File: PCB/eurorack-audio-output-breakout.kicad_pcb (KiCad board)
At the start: 2 copper layers, 18.4 x 50.5 mm, 12 parts, among them J1 Conn_01x04_Pin, J10 A, J11 B, J12 Conn_01x05_Pin, J3 Conn_01x04_Pin, J4 Conn_01x02_Pin, J5 Conn_01x05_Pin, U1 TL072

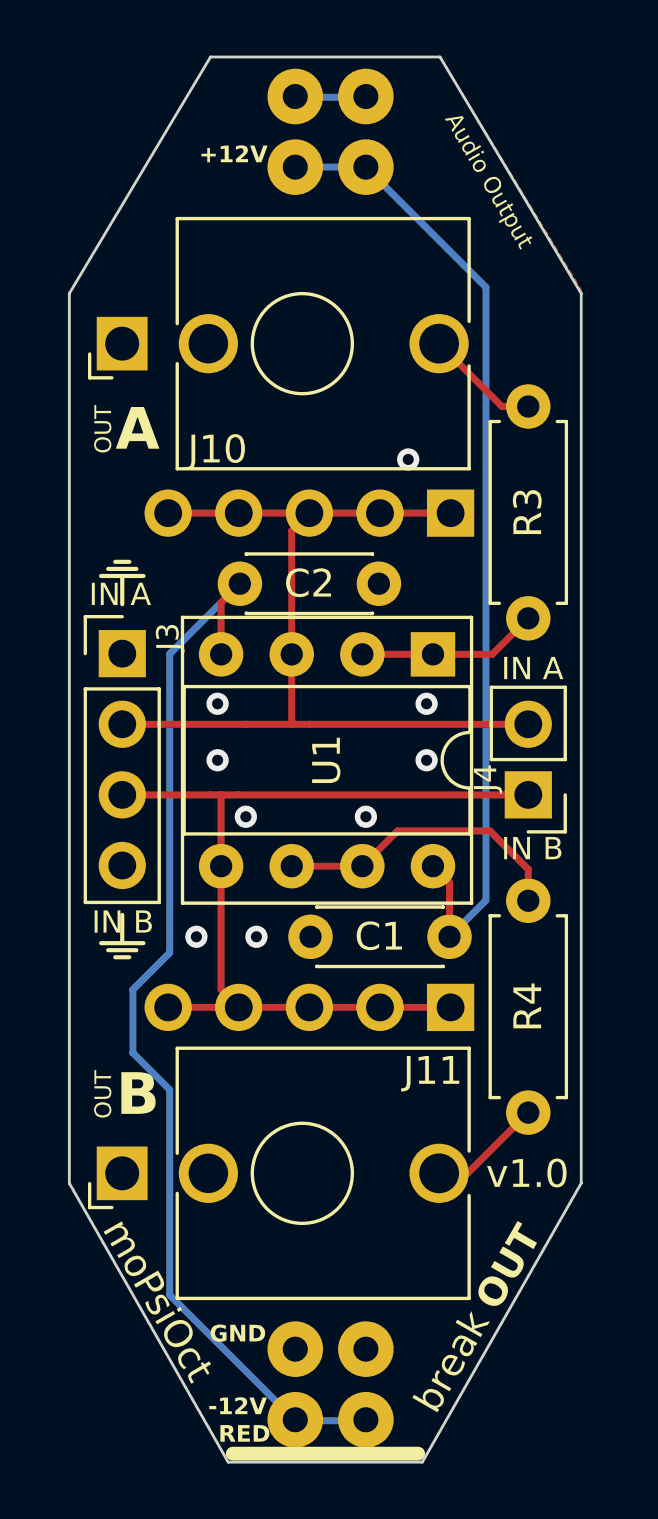
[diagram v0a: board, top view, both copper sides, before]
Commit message: Fix header and text placement
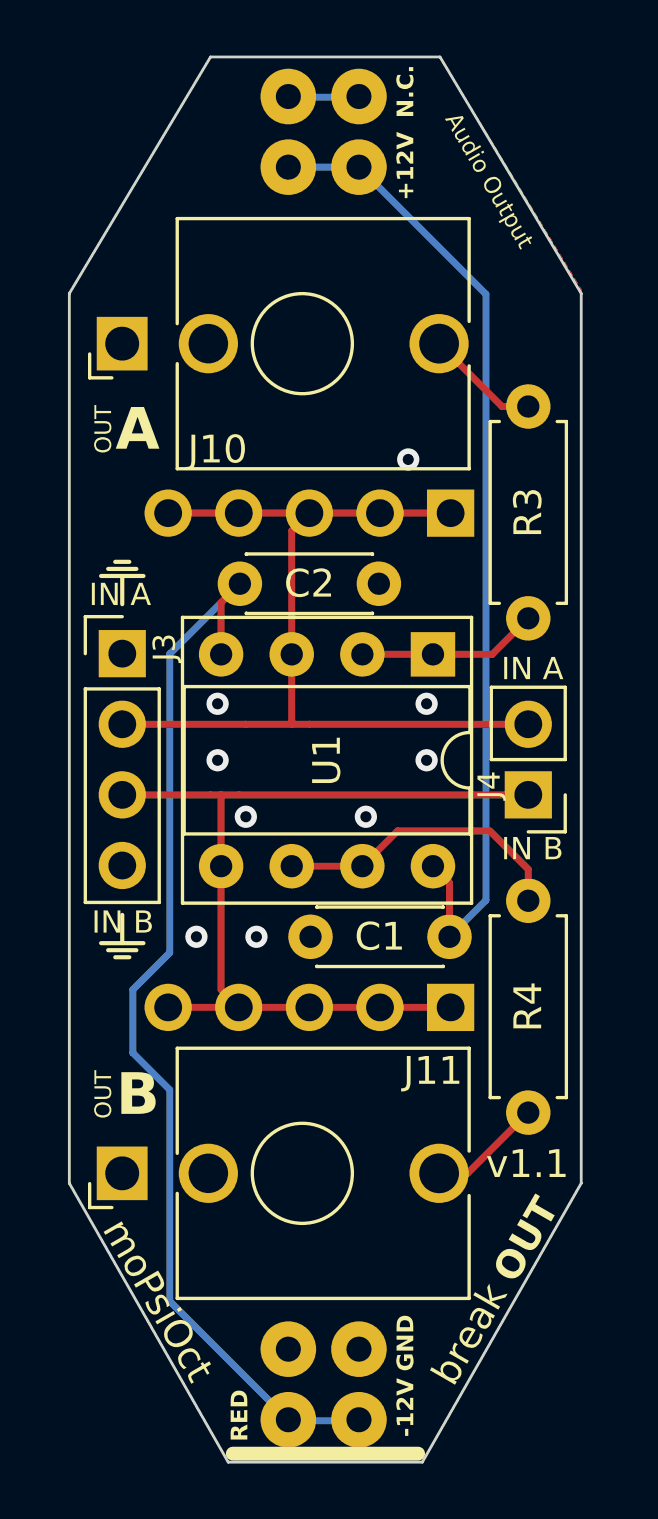
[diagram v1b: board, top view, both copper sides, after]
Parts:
- moved J1 0.25 mm to (191.8, 88.8)
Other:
- board text added: "N.C."
- board text added: "v1.1"
- board text removed: "v1.0"
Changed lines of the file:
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@@
 				(font
 					(size 1.27 1.27)
+					(thickness 0.15)
 				)
 			)
@@
 				(font
 					(size 1.27 1.27)
+					(thickness 0.15)
 				)
 			)
@@
 				(font
 					(size 1.27 1.27)
+					(thickness 0.15)
 				)
 			)
@@
 				(font
 					(size 1.27 1.27)
+					(thickness 0.15)
 				)
 			)
@@
 				(font
 					(size 1.27 1.27)
+					(thickness 0.15)
 				)
 			)
@@
 				(font
 					(size 1.27 1.27)
+					(thickness 0.15)
 				)
 			)
@@
 		(tags "Through hole pin header THT 1x04 2.54mm single row")
 		(property "Reference" "J3"
-			(at 1.651 -0.6096 90)
+			(at 1.524 -0.2286 90)
 			(layer "F.SilkS")
 			(effects
@@
 				(font
 					(size 1.27 1.27)
+					(thickness 0.15)
 				)
 			)
@@
 				(font
 					(size 1.27 1.27)
+					(thickness 0.15)
 				)
 			)
@@
 				(font
 					(size 1.27 1.27)
+					(thickness 0.15)
 				)
 			)
@@
 				(font
 					(size 1.27 1.27)
+					(thickness 0.15)
 				)
 			)
@@
 				(font
 					(size 1.27 1.27)
+					(thickness 0.15)
 				)
 			)
@@
 				(font
 					(size 1.27 1.27)
+					(thickness 0.15)
 				)
 			)
@@
 				(font
 					(size 1.27 1.27)
+					(thickness 0.15)
 				)
 			)
@@
 				(font
 					(size 1.27 1.27)
+					(thickness 0.15)
 				)
 			)
@@
 				(font
 					(size 1.27 1.27)
+					(thickness 0.15)
 				)
 			)
@@
 				(font
 					(size 1.27 1.27)
+					(thickness 0.15)
 				)
 			)
@@
 				(font
 					(size 1.27 1.27)
+					(thickness 0.15)
 				)
 			)
@@
 				(font
 					(size 1.27 1.27)
+					(thickness 0.15)
 				)
 			)
@@
 		(tags "Through hole pin header THT 1x02 2.54mm single row")
 		(property "Reference" "J4"
-			(at 1.524 0.6096 90)
+			(at 1.397 0.3556 90)
 			(layer "F.SilkS")
 			(effects
@@
 				(font
 					(size 1.27 1.27)
+					(thickness 0.15)
 				)
 			)
@@
 				(font
 					(size 1.27 1.27)
+					(thickness 0.15)
 				)
 			)
@@
 				(font
 					(size 1.27 1.27)
+					(thickness 0.15)
 				)
 			)
@@
 				(font
 					(size 1.27 1.27)
+					(thickness 0.15)
 				)
 			)
@@
 				(font
 					(size 1.27 1.27)
+					(thickness 0.15)
 				)
 			)
@@
 				(font
 					(size 1.27 1.27)
+					(thickness 0.15)
 				)
 			)
@@
 				(font
 					(size 1.27 1.27)
+					(thickness 0.15)
 				)
 			)
@@
 				(font
 					(size 1.27 1.27)
+					(thickness 0.15)
 				)
 			)
@@
 				(font
 					(size 1.27 1.27)
+					(thickness 0.15)
 				)
 			)
@@
 				(font
 					(size 1.27 1.27)
+					(thickness 0.15)
 				)
 			)
@@
 				(font
 					(size 1.27 1.27)
+					(thickness 0.15)
 				)
 			)
@@
 				(font
 					(size 1.27 1.27)
+					(thickness 0.15)
 				)
 			)
@@
 				(font
 					(size 1.27 1.27)
+					(thickness 0.15)
 				)
 			)
@@
 				(font
 					(size 1.27 1.27)
+					(thickness 0.15)
 				)
 			)
@@
 				(font
 					(size 1.27 1.27)
+					(thickness 0.15)
 				)
 			)
@@
 	)
 	(footprint "moPsy:Breadboard Power Connector"
-		(locked yes)
 		(layer "B.Cu")
-		(at 192.019 88.824 180)
+		(at 191.77 88.824 180)
 		(property "Reference" "J1"
 			(at 0.757 19.101 0)
@@
 				(font
 					(size 1.27 1.27)
+					(thickness 0.15)
 				)
 			)
@@
 				(font
 					(size 1.27 1.27)
+					(thickness 0.15)
 				)
 			)
@@
 				(font
 					(size 1.27 1.27)
+					(thickness 0.15)
 				)
 			)
@@
 	)
 	(gr_text "RED"
-		(at 187.2234 113.4872 0)
+		(at 188.341 113.411 90)
 		(layer "F.SilkS")
 		(effects
@@
 	)
 	(gr_text "+12V"
-		(at 189.0014 67.4624 0)
+		(at 194.31 66.294 90)
 		(layer "F.SilkS")
 		(effects
@@
 	)
 	(gr_text "break"
-		(at 195.1482 112.522 60)
+		(at 195.7832 111.5314 60)
 		(layer "F.SilkS")
 		(effects
@@
 		)
 	)
-	(gr_text "v1.0"
-		(at 196.85 104.3686 0)
+	(gr_text "v1.1"
+		(at 196.85 104.013 0)
 		(layer "F.SilkS")
 		(effects
@@
 	)
 	(gr_text "OUT"
-		(at 197.358 108.8136 60)
+		(at 197.993 107.823 60)
 		(layer "F.SilkS")
 		(effects
@@
 		)
 	)
+	(gr_text "N.C."
+		(at 194.31 63.881 90)
+		(layer "F.SilkS")
+		(effects
+			(font
+				(size 0.6 0.6)
+				(thickness 0.1)
+				(bold yes)
+			)
+			(justify right bottom)
+		)
+	)
 	(gr_text "OUT"
 		(at 183.4388 77.8764 90)
@@
 	)
 	(gr_text "-12V"
-		(at 188.976 112.4966 0)
+		(at 194.31 111.125 90)
 		(layer "F.SilkS")
 		(effects
@@
 	)
 	(gr_text "GND"
-		(at 188.9506 109.8804 0)
+		(at 194.31 108.839 90)
 		(layer "F.SilkS")
 		(effects
@@
 	)
 	(segment
-		(start 196.85 71.882)
-		(end 196.85 93.94)
+		(start 196.85 93.94)
+		(end 195.54 95.25)
 		(width 0.25)
 		(layer "B.Cu")
@@
 	)
 	(segment
-		(start 189.992 67.564)
-		(end 192.532 67.564)
+		(start 192.283 67.564)
+		(end 196.85 72.131)
 		(width 0.25)
 		(layer "B.Cu")
@@
 	)
 	(segment
-		(start 196.85 93.94)
-		(end 195.54 95.25)
+		(start 196.85 72.131)
+		(end 196.85 93.94)
 		(width 0.25)
 		(layer "B.Cu")
@@
 	)
 	(segment
-		(start 192.532 67.564)
-		(end 196.85 71.882)
+		(start 189.743 67.564)
+		(end 192.283 67.564)
 		(width 0.25)
 		(layer "B.Cu")
@@
 	)
 	(segment
-		(start 185.476 85.074)
-		(end 188 82.55)
+		(start 185.476 95.823649)
+		(end 185.476 85.074)
 		(width 0.25)
 		(layer "B.Cu")
@@
 	)
 	(segment
-		(start 189.997 112.6596)
-		(end 185.476 108.1386)
+		(start 192.537 112.6596)
+		(end 189.7786 112.6596)
 		(width 0.25)
 		(layer "B.Cu")
@@
 	)
 	(segment
-		(start 185.476 100.7546)
-		(end 184.15 99.4286)
+		(start 184.15 97.149649)
+		(end 185.476 95.823649)
+		(width 0.25)
+		(layer "B.Cu")
+		(net 3)
+	)
+	(segment
+		(start 184.15 99.4286)
+		(end 184.15 97.149649)
 		(width 0.25)
 		(layer "B.Cu")
@@
 	)
 	(segment
-		(start 185.476 108.1386)
+		(start 185.476 108.357)
 		(end 185.476 100.7546)
 		(width 0.25)
@@
 	)
 	(segment
-		(start 184.15 97.149649)
-		(end 185.476 95.823649)
+		(start 189.743 112.624)
+		(end 185.476 108.357)
 		(width 0.25)
 		(layer "B.Cu")
@@
 	)
 	(segment
-		(start 184.15 99.4286)
-		(end 184.15 97.149649)
+		(start 185.476 85.074)
+		(end 188 82.55)
 		(width 0.25)
 		(layer "B.Cu")
@@
 	)
 	(segment
-		(start 192.537 112.6596)
-		(end 189.997 112.6596)
+		(start 185.476 100.7546)
+		(end 184.15 99.4286)
 		(width 0.25)
 		(layer "B.Cu")
@@
 	)
 	(segment
-		(start 185.476 95.823649)
-		(end 185.476 85.074)
+		(start 189.7786 112.6596)
+		(end 189.743 112.624)
 		(width 0.25)
 		(layer "B.Cu")
